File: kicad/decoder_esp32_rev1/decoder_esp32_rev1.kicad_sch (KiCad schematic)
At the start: 49 parts, among them J1 TRCK_IN, J2 F_2, J3 F_3, J4 F_1, J5 F_4, J6 AUX_5V, J8 MTR_OUT, J9 to_cap_brd, Q1 BSS138, Q2 BSS138, Q3 BSS138, Q4 BSS138, U1 ESP32-C3_SUPERMINI_TH, U2 LM2596S-5, U3 TB67H450FNG_EL

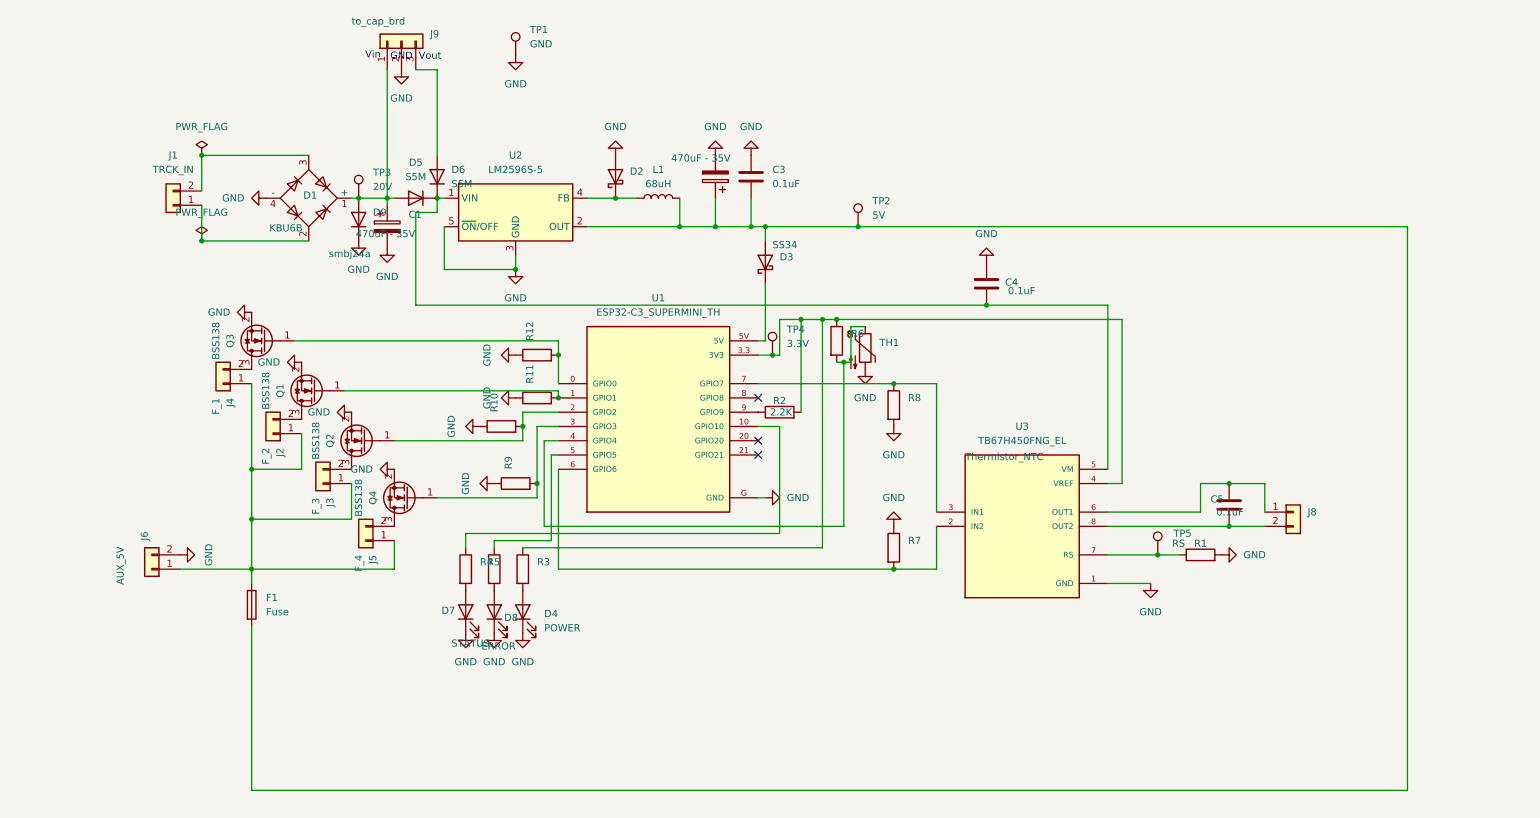
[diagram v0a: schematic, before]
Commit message: KiCad rev3: schematic/PCB layout reorganization + remove PWR_FLAG symbols
Reordered components and wiring for better schematic overview.
Removed #FLG01/#FLG02 PWR_FLAG symbols (cosmetic ERC cleanup).
No netlist or component value changes.

Co-Authored-By: Claude Sonnet 4.6 <noreply@anthropic.com>
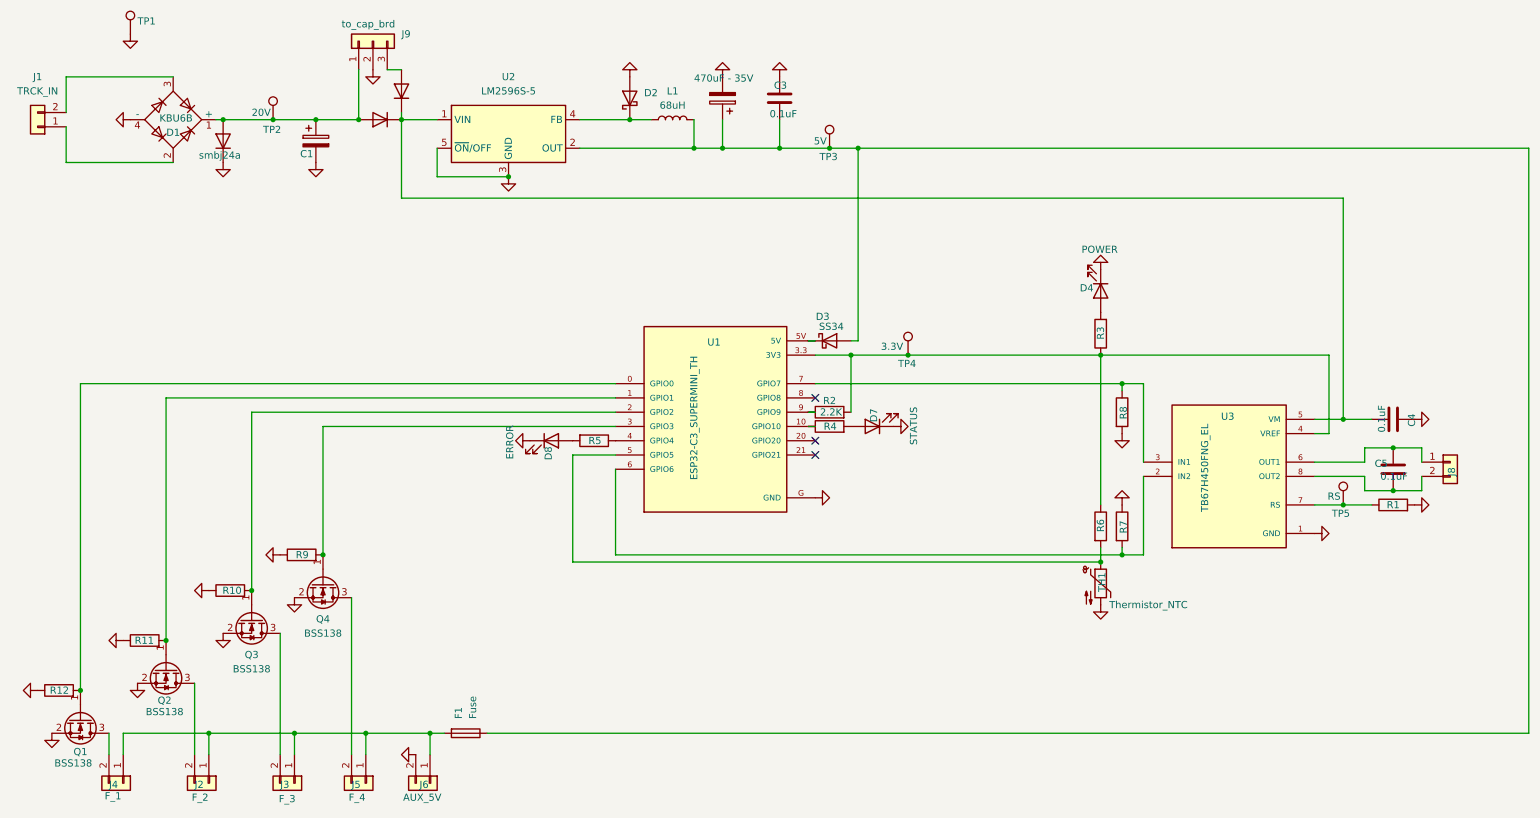
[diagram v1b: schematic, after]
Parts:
- C1: value 470uF - 35V -> (none)
- renumbered Q3 to Q1, Q1 to Q2, Q2 to Q3, TP3 to TP2, TP2 to TP3
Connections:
- net at C2.1, C3.2, D3.2 (A)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: now also F1.1; no longer F1.2
- net at J2.1 (Pin_1), J3.1 (Pin_1), J4.1 (Pin_1)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: now also F1.2; no longer F1.1
- net at R6.2, TH1.1: now also U1.5 (GPIO5); no longer U1.4 (GPIO4)
- net at R5.1: now also U1.4 (GPIO4); no longer U1.5 (GPIO5)
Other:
- note removed: "GND"
- note removed: "Vin"
- note removed: "Vout"
- moved on the sheet: C1, C3, C5, D1, D2, D3, F1, J1, J2, J3, J4, J5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

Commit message: KiCad sch: reposition ERROR LED circuit for readability
Moved D8 + R5 + GND symbol to a cleaner area of the canvas.
No connectivity or value changes.

Co-Authored-By: Claude Sonnet 4.6 <noreply@anthropic.com>
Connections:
- net at R6.2, TH1.1: now also U1.4 (GPIO4); no longer U1.5 (GPIO5)
- net at R5.1: now also U1.5 (GPIO5); no longer U1.4 (GPIO4)
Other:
- moved on the sheet: D8, R5
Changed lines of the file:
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@@
+	(wire
+		(pts
+			(xy 104.14 93.98) (xy 119.38 93.98)
+		)
+		(stroke
+			(width 0)
+			(type default)
+		)
+	)
 	(wire
 		(pts
@@
 	(wire
 		(pts
-			(xy 111.76 93.98) (xy 119.38 93.98)
-		)
-		(stroke
-			(width 0)
-			(type default)
-		)
-	)
-	(wire
-		(pts
 			(xy 81.28 34.29) (xy 87.63 34.29)
 		)
@@
 	(wire
 		(pts
+			(xy 111.76 91.44) (xy 119.38 91.44)
+		)
+		(stroke
+			(width 0)
+			(type default)
+		)
+	)
+	(wire
+		(pts
 			(xy 119.38 111.76) (xy 119.38 96.52)
 		)
@@
 	(wire
 		(pts
-			(xy 111.76 113.03) (xy 111.76 93.98)
-		)
-		(stroke
-			(width 0)
-			(type default)
-		)
-	)
-	(wire
-		(pts
 			(xy 138.43 34.29) (xy 138.43 39.37)
 		)
@@
 		(pts
 			(xy 254 102.87) (xy 248.92 102.87)
+		)
+		(stroke
+			(width 0)
+			(type default)
+		)
+	)
+	(wire
+		(pts
+			(xy 111.76 91.44) (xy 111.76 113.03)
 		)
 		(stroke
@@
 	(symbol
 		(lib_id "Device:LED")
-		(at 107.95 91.44 0)
+		(at 92.71 93.98 0)
 		(unit 1)
 		(body_style 1)
@@
 		(dnp no)
 		(property "Reference" "D8"
-			(at 107.442 92.456 90)
+			(at 92.202 94.996 90)
 			(show_name no)
 			(do_not_autoplace no)
@@
 		)
 		(property "Value" "ERROR"
-			(at 100.584 88.646 90)
+			(at 85.344 91.186 90)
 			(show_name no)
 			(do_not_autoplace no)
@@
 		)
 		(property "Footprint" "Diode_SMD:D_1206_3216Metric_Pad1.42x1.75mm_HandSolder"
-			(at 107.95 91.44 0)
+			(at 92.71 93.98 0)
 			(hide yes)
 			(show_name no)
@@
 		)
 		(property "Datasheet" ""
-			(at 107.95 91.44 0)
+			(at 92.71 93.98 0)
 			(hide yes)
 			(show_name no)
@@
 		)
 		(property "Description" "Light emitting diode"
-			(at 107.95 91.44 0)
+			(at 92.71 93.98 0)
 			(hide yes)
 			(show_name no)
@@
 		)
 		(property "Sim.Pins" "1=K 2=A"
-			(at 107.95 91.44 0)
+			(at 92.71 93.98 0)
 			(hide yes)
 			(show_name no)
@@
 	(symbol
 		(lib_id "power:GND")
-		(at 104.14 91.44 270)
+		(at 88.9 93.98 270)
 		(unit 1)
 		(body_style 1)
@@
 		(fields_autoplaced yes)
 		(property "Reference" "#PWR017"
-			(at 97.79 91.44 0)
+			(at 82.55 93.98 0)
 			(hide yes)
 			(show_name no)
@@
 		)
 		(property "Value" "GND"
-			(at 99.06 91.44 0)
+			(at 83.82 93.98 0)
 			(hide yes)
 			(show_name no)
@@
 		)
 		(property "Footprint" ""
-			(at 104.14 91.44 0)
+			(at 88.9 93.98 0)
 			(hide yes)
 			(show_name no)
@@
 		)
 		(property "Datasheet" ""
-			(at 104.14 91.44 0)
+			(at 88.9 93.98 0)
 			(hide yes)
 			(show_name no)
@@
 		)
 		(property "Description" "Power symbol creates a global label with name \"GND\" , ground"
-			(at 104.14 91.44 0)
+			(at 88.9 93.98 0)
 			(hide yes)
 			(show_name no)
@@
 	(symbol
 		(lib_id "Device:R")
-		(at 115.57 91.44 270)
+		(at 100.33 93.98 270)
 		(unit 1)
 		(body_style 1)
@@
 		(dnp no)
 		(property "Reference" "R5"
-			(at 114.554 91.44 90)
+			(at 99.314 93.98 90)
 			(show_name no)
 			(do_not_autoplace no)
@@
 		)
 		(property "Value" "Red ERROR 150Ohm"
-			(at 114.3001 93.98 0)
+			(at 99.0601 96.52 0)
 			(hide yes)
 			(show_name no)
@@
 		)
 		(property "Footprint" "Resistor_SMD:R_1206_3216Metric_Pad1.30x1.75mm_HandSolder"
-			(at 115.57 89.662 90)
+			(at 100.33 92.202 90)
 			(hide yes)
 			(show_name no)
@@
 		)
 		(property "Datasheet" ""
-			(at 115.57 91.44 0)
+			(at 100.33 93.98 0)
 			(hide yes)
 			(show_name no)
@@
 		)
 		(property "Description" "Resistor"
-			(at 115.57 91.44 0)
-			(hide yes)
-			(show_name no)
+			(at 100.33 93.98 0)
+			(hide yes)
+			(show_name no)
